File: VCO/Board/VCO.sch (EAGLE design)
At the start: 57 parts, among them IC1 AD711N, IC2 AD711N, IC3 AD711N, IC4 AD711N, IC5 AD711N, T1 BC337, T2 BC337

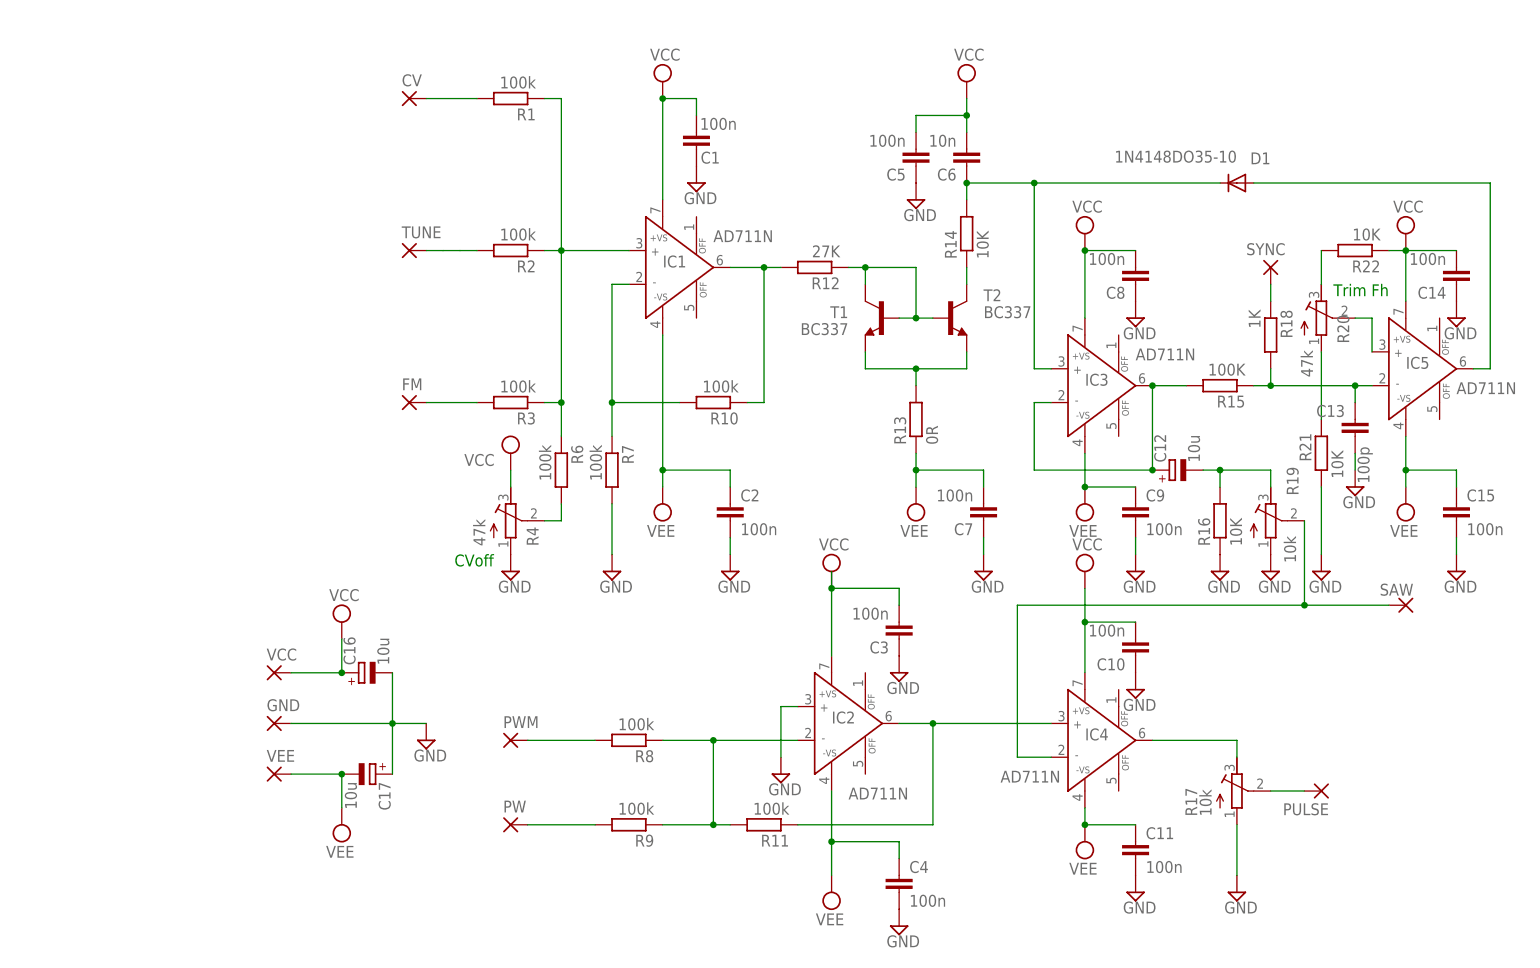
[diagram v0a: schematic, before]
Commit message: Change VCO connectors
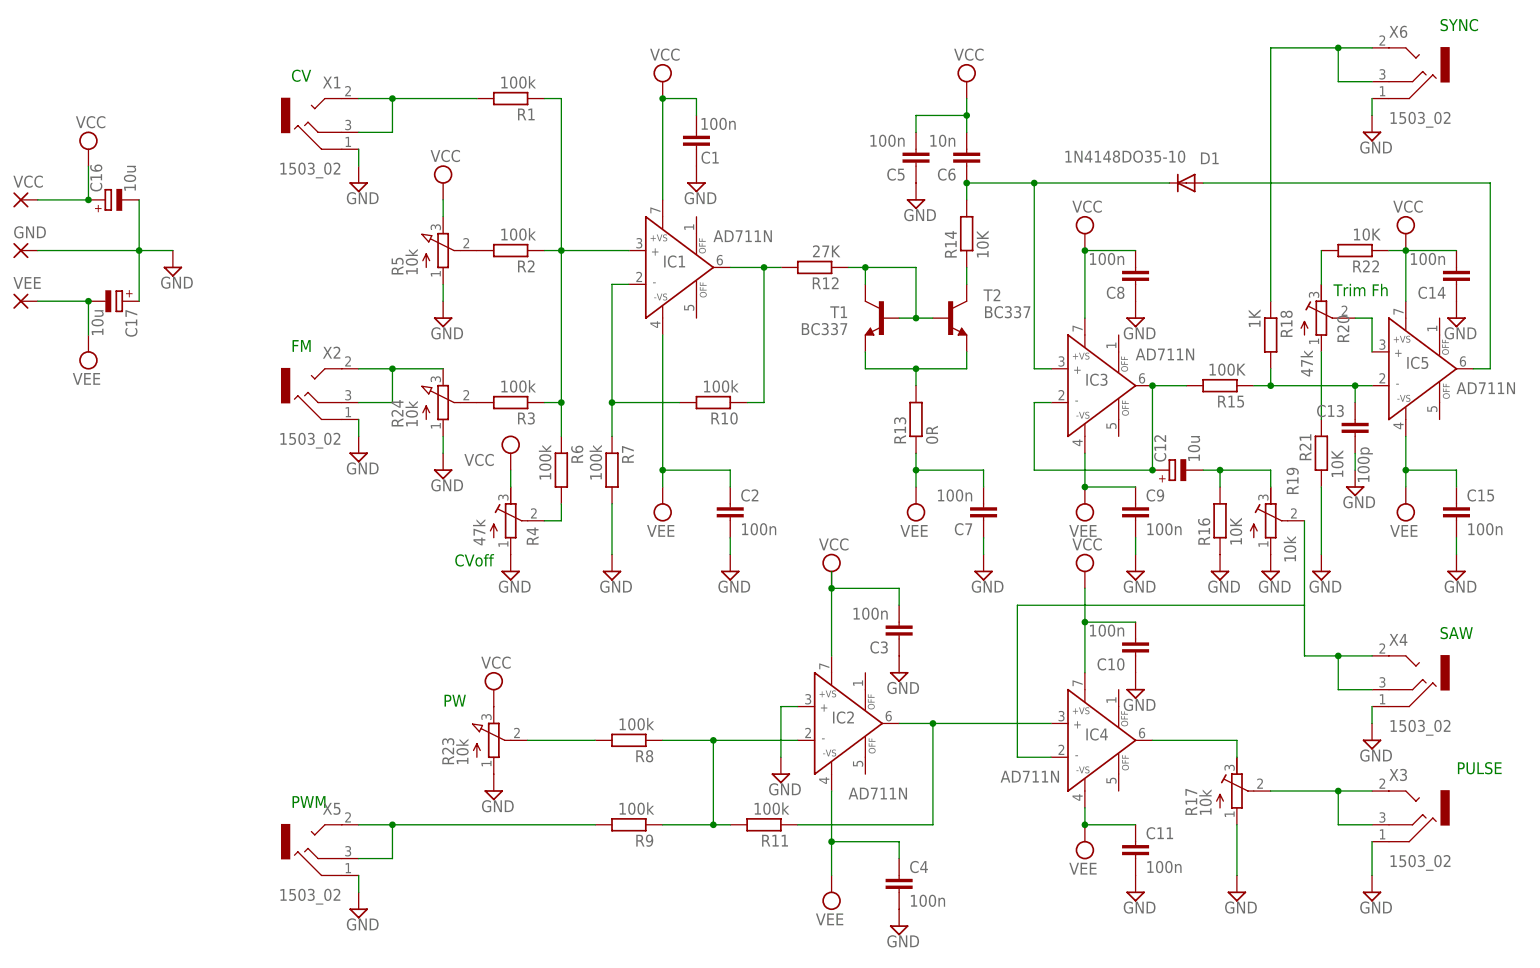
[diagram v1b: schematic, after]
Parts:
- removed CV, FM, PULSE, PW, PWM, SAW, SYNC, TUNE: (no value), wirepad:3,17/1,1
- added R23, R24, R5: 10k, pot:3RP/1610N
- added X1, X2, X3, X4, X5, X6: 1503_02, con-lumberg:1503_02
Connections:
- new net N$26: R24.E, X2.2, X2.3
- net GND: now also R23.A, R24.A, R5.A, X1.1, X2.1, X3.1, X4.1, X5.1, X6.1
- net N$12: now also X1.2, X1.3; no longer CV.P
- net N$14: now also R24.S; no longer FM.P
- net N$15: now also X6.2, X6.3; no longer SYNC.P
- net N$17: now also R5.S; no longer TUNE.P
- net N$21: now also X4.2, X4.3; no longer SAW.P
- net N$23: now also X3.3; no longer PULSE.P
- net N$27: now also R23.S; no longer PWM.P
- net N$28: now also X5.2, X5.3; no longer PW.P
- net VCC: now also R23.E, R5.E
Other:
- note added: "CV"
- note added: "FM"
- note added: "PULSE"
- note added: "PW"
- note added: "PWM"
- note added: "SAW"
- note added: "SYNC"
- moved on the sheet: C16, C17, D1, GND, VCC, VEE

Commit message: Change VCO to use TL074
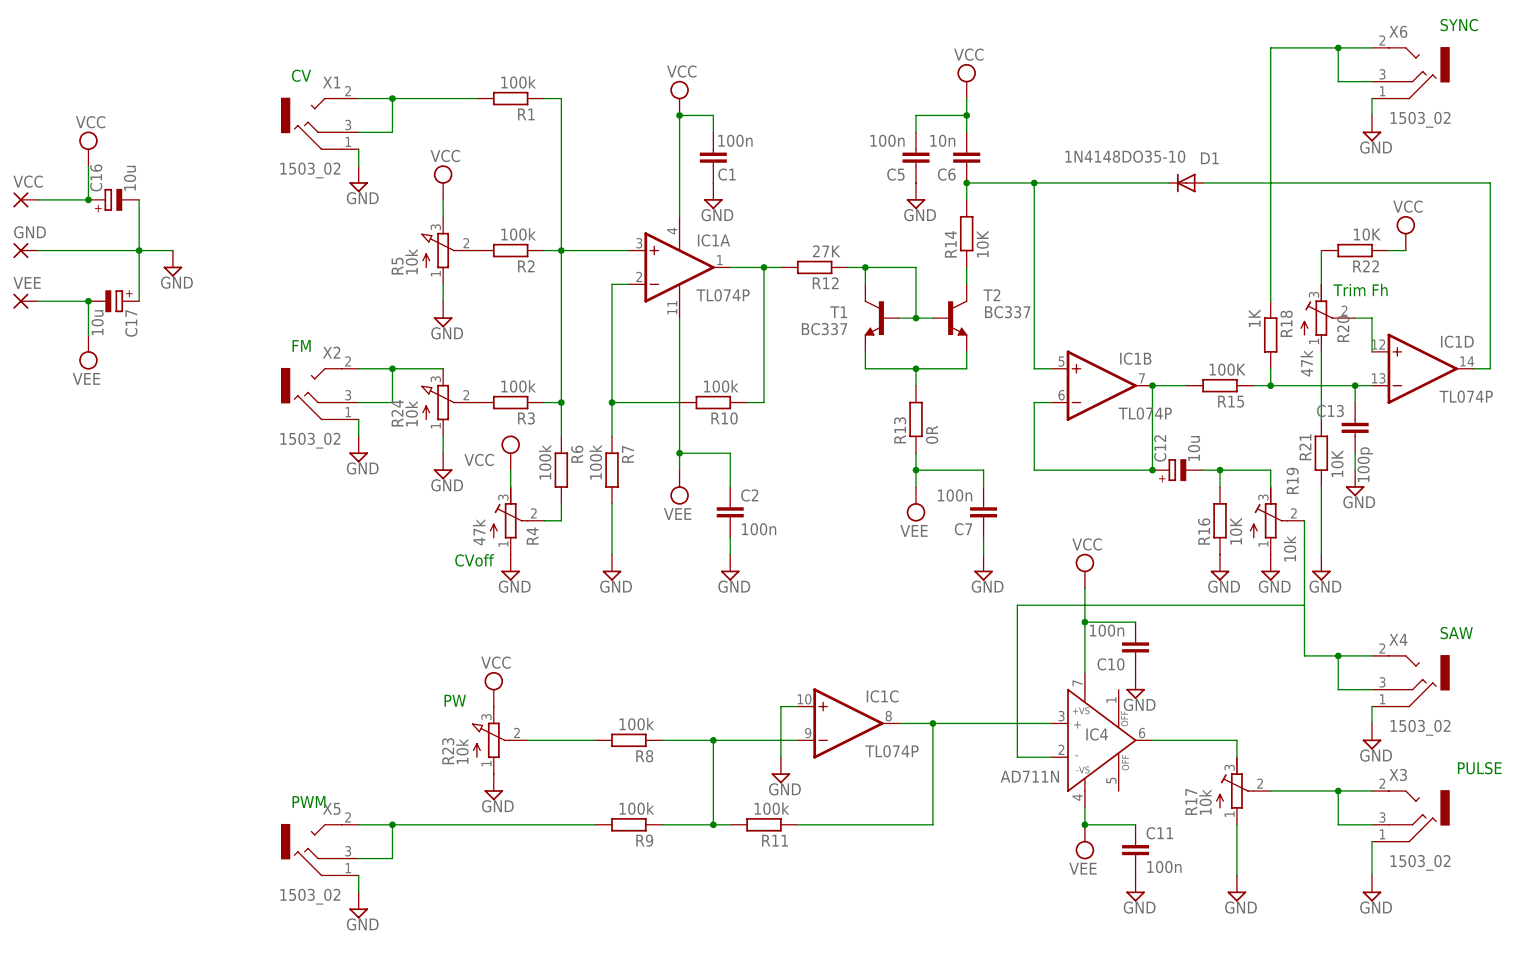
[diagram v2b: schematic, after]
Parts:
- removed C14, C15, C3, C4, C8, C9: 100n, capacitor-wima:C5/2.5
- removed IC2, IC3, IC5: AD711N, analog-devices:AD711N
- IC1: value AD711N -> TL074P; device analog-devices:AD711N -> linear:TL074P
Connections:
- net GND: now also IC1C.+IN; no longer C14.1, C15.2, C3.1, C4.2, C8.1, C9.2, IC2.IN+
- net N$13: now also IC1A.+IN; no longer IC1.IN+
- net N$18: now also IC1A.OUT; no longer IC1.OUT
- net N$20: now also IC1A.-IN; no longer IC1.IN-
- net N$24: now also IC1C.-IN; no longer IC2.IN-
- net N$29: now also IC1C.OUT; no longer IC2.OUT
- net N$3: now also IC1B.+IN; no longer IC3.IN+
- net N$5: now also IC1D.OUT; no longer IC5.OUT
- net N$6: now also IC1D.+IN; no longer IC5.IN+
- net N$7: now also IC1D.-IN; no longer IC5.IN-
- net N$8: now also IC1B.-IN, IC1B.OUT; no longer IC3.IN-, IC3.OUT
- net VCC: no longer C14.2, C3.2, C8.2, IC1.+VS, IC2.+VS, IC3.+VS, IC5.+VS
- net VEE: no longer C15.1, C4.1, C9.1, IC1.-VS, IC2.-VS, IC3.-VS, IC5.-VS
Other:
- moved on the sheet: C1

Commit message: Tweks to reduce BOM cost
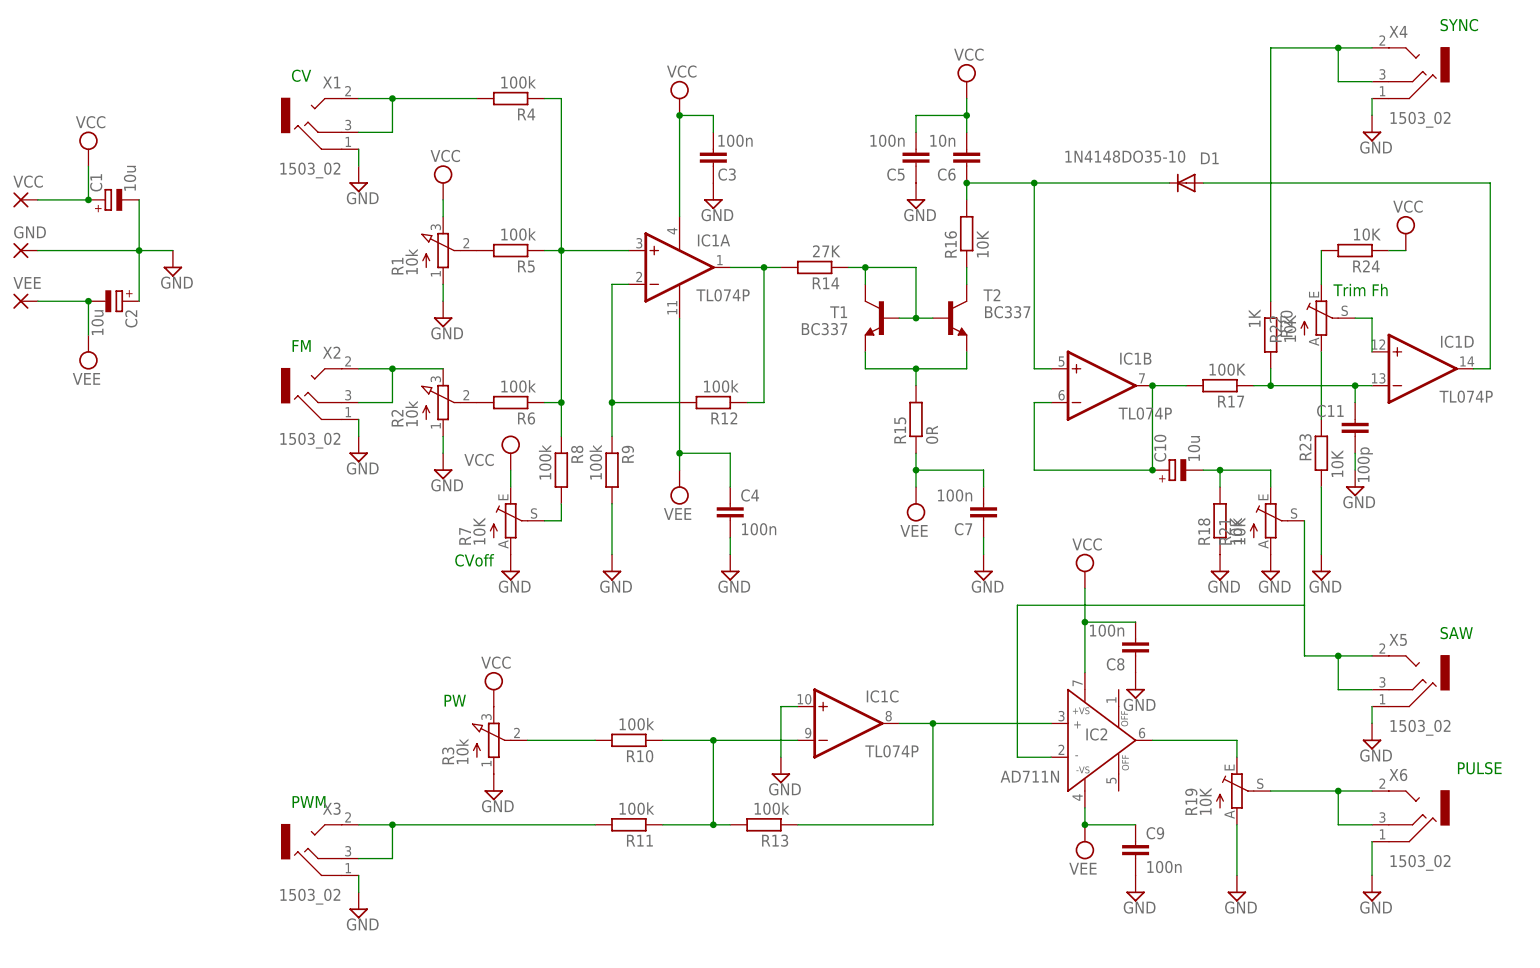
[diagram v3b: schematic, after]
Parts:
- removed C12, C16, C17: 10u, rcl:CPOL-EUE2.5-7
- removed C13: 100p, capacitor-wima:C2.5/2
- added C3, C4, C8, C9: 100n, capacitor-wima:C5/2.5
- C1, C10, C2: value 100n -> 10u; device capacitor-wima:C5/2.5 -> rcl:CPOL-EUE2.5-7
- C11: value 100n -> 100p; device capacitor-wima:C5/2.5 -> capacitor-wima:C2.5/2
- R1, R2, R3: value 100k -> 10k; device eagle-ltspice:R0207/10 -> pot:3RP/1610N; SPICEPREFIX 27K -> (none)
- R12: value 27K -> 100k
- R13: value 0R -> 100k; SPICEPREFIX (none) -> 27K
- R14: value 10K -> 27K; SPICEPREFIX 10K -> 27K
- R15: value 100K -> 0R
- R17: value 10k -> 100K; device resistor:R-TRIMM3339P -> eagle-ltspice:R0207/10
- R18: value 1K -> 10K; SPICEPREFIX (none) -> 10K
- R19: value 10k -> 10K; device resistor:R-TRIMM3339P -> pot:TRIM_EU-CA6V
- R20: value 47k -> 1K; device rcl:R-TRIMM64W -> eagle-ltspice:R0207/10
- R21, R22: device eagle-ltspice:R0207/10 -> pot:TRIM_EU-CA6V; SPICEPREFIX 10K -> (none)
- R23, R24: value 10k -> 10K; device pot:3RP/1610N -> eagle-ltspice:R0207/10; SPICEPREFIX (none) -> 10K
- R4: value 47k -> 100k; device rcl:R-TRIMM64W -> eagle-ltspice:R0207/10; SPICEPREFIX (none) -> 27K
- R5: value 10k -> 100k; device pot:3RP/1610N -> eagle-ltspice:R0207/10; SPICEPREFIX (none) -> 27K
- R7: value 100k -> 10K; device eagle-ltspice:R0207/10 -> pot:TRIM_EU-CA6V; SPICEPREFIX 27K -> (none)
- renumbered IC4 to IC2
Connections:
- net GND: now also C1.-, C11.1, C2.+, C3.1, C4.2, C8.1, C9.2, R1.A, R18.1, R2.A, R21.A, R23.1, R3.A, R7.A, R9.2; no longer C1.1, C10.1, C11.2, C13.1, C16.-, C17.+, C2.2, R16.1, R17.A, R21.1, R23.A, R24.A, R4.A, R5.A, R7.2
- net N$1: now also R14.1; no longer R12.1
- net N$10: now also R7.S, R8.2; no longer R4.S, R6.2
- net N$11: now also R22.E, R24.2; no longer R20.E, R22.2
- net N$12: now also R4.2; no longer R1.2
- net N$13: now also R4.1, R5.1, R8.1; no longer R1.1, R2.1, R3.1
- net N$14: now also R2.S, R6.2; no longer R24.S, R3.2
- net N$15: now also R20.1, X4.2, X4.3; no longer R18.1, X6.2, X6.3
- net N$17: now also R1.S, R5.2; no longer R2.2, R5.S
- net N$18: now also R12.1, R14.2; no longer R10.1, R12.2
- net N$2: now also R15.2; no longer R13.2
- net N$20: now also R12.2, R9.1; no longer R10.2, R7.1
- net N$21: now also R21.S, X5.2, X5.3; no longer R19.S, X4.2, X4.3
- net N$22: now also R19.E; no longer R17.E
- net N$23: now also R19.S, X6.3; no longer R17.S, X3.3
- net N$24: now also R10.1, R11.1, R13.2; no longer R11.2, R8.1, R9.1
- net N$25: now also C10.-, R18.2, R21.E; no longer C12.-, R16.2, R19.E
- net N$26: now also R2.E; no longer R24.E
- net N$27: now also R10.2, R3.S; no longer R23.S, R8.2
- net N$28: now also R11.2, X3.2, X3.3; no longer R9.2, X5.2, X5.3
- net N$29: now also R13.1; no longer R11.1
- net N$3: now also R16.2; no longer R14.2
- net N$4: now also R16.1; no longer R14.1
- net N$6: now also R22.S; no longer R20.S
- net N$7: now also C11.2, R17.1, R20.2; no longer C13.2, R15.1, R18.2
- net N$8: now also C10.+, R17.2; no longer C12.+, R15.2
- net N$9: now also R22.A, R23.2; no longer R20.A, R21.2
- net VCC: now also C1.+, C3.2, C8.2, R1.E, R24.1, R3.E, R7.E; no longer C1.2, C10.2, C16.+, R22.1, R23.E, R4.E, R5.E
- net VEE: now also C2.-, C4.1, C9.1, R15.1; no longer C11.1, C17.-, C2.1, R13.1
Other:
- moved on the sheet: C11, R10, R11, R12, R13, R14, R15, R16, R18, R6, R8, R9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
